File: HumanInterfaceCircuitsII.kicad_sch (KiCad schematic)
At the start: 45 parts

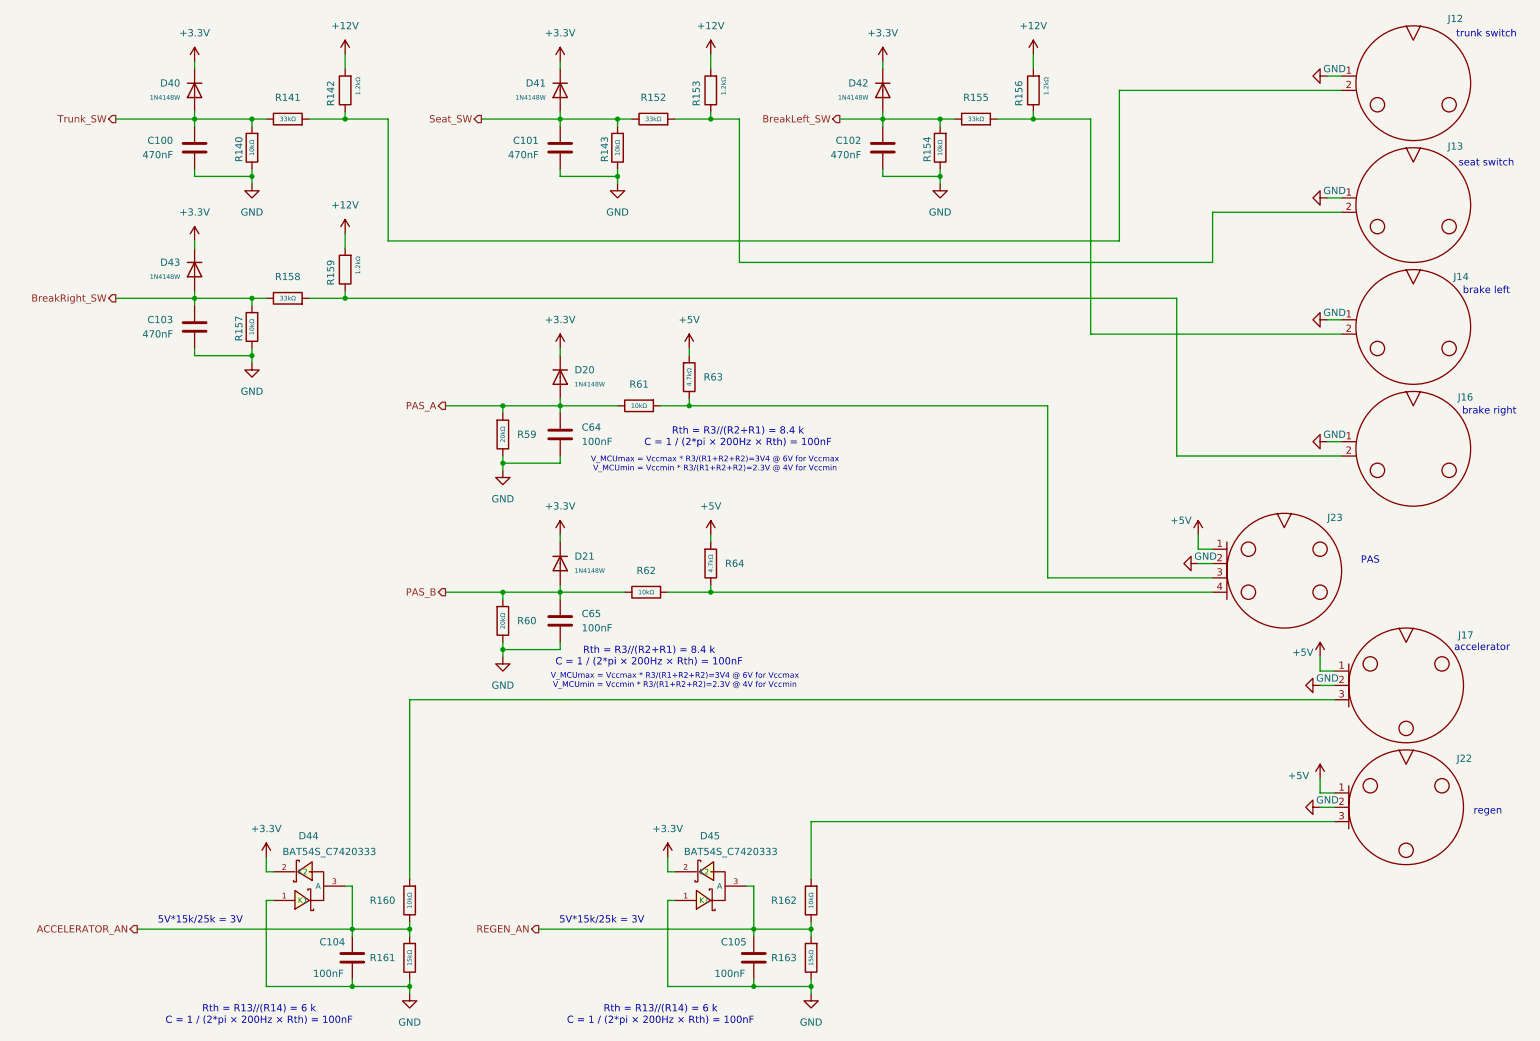
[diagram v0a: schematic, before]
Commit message: EMI/EMC meassures implementation + VCU panel interface block
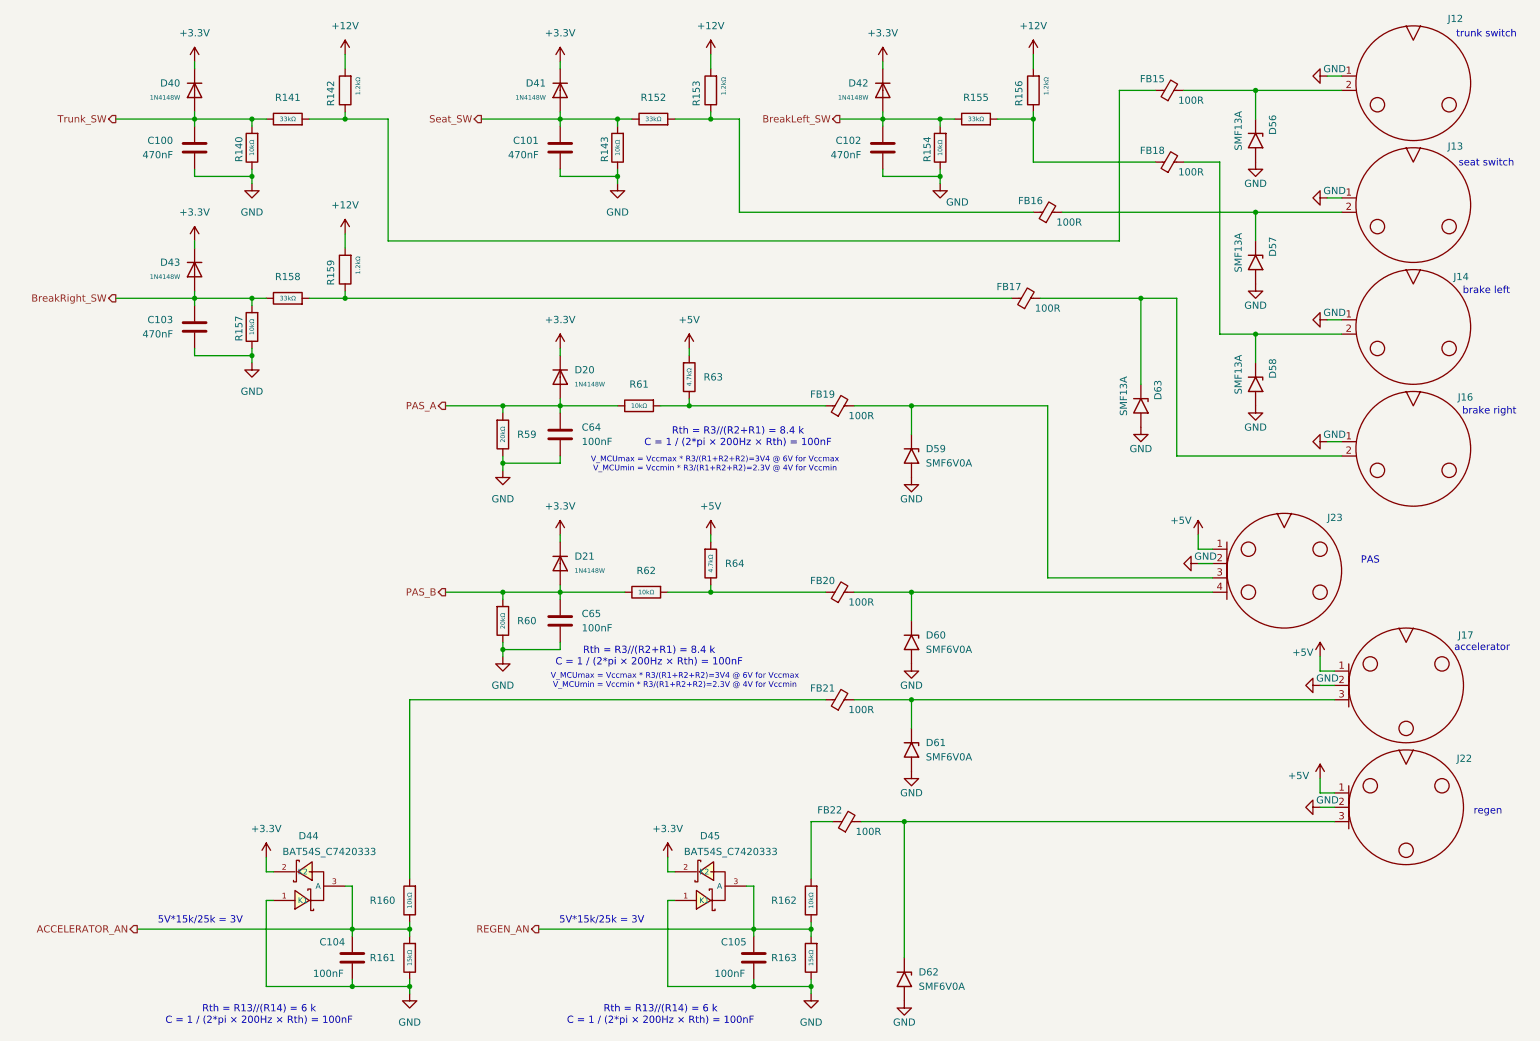
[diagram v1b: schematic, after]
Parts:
- added D56, D57, D58, D63: SMF13A, Diode_SMD:D_SMF, symbol VELION_VCU_Library:SMF13A
- added D59, D60, D61, D62: SMF6V0A, Diode_SMD:D_SMF, symbol VELION_VCU_Library:SMF6V0A
- added FB15, FB16, FB17, FB18, FB19, FB20, FB21, FB22: 100R, Inductor_SMD:L_0603_1608Metric, symbol VELION_VCU_Library:FerriteBead_Small
- C100, C101, C102, C103, C104, C105, C64, C65: footprint (none) -> Capacitor_SMD:C_0603_1608Metric; symbol Device:C -> VELION_VCU_Library:C
- D20, D21, D40, D41, D42, D43: footprint PCM_JLCPCB:D_SOD-123 -> Diode_SMD:D_SOD-123; symbol PCM_JLCPCB-Diodes:Switching,1N4148W -> VELION_VCU_Library:Switching,1N4148W
- D44, D45: footprint PCM_JLCPCB:SOT-23-3_L2.9-W1.3-P1.90-LS2.4-BR -> Package_TO_SOT_SMD:SOT-23-3; symbol PCM_JLCPCB-Diode-Packages:Schottky, BAT54S_C7420333 -> VELION_VCU_Library:Schottky, BAT54S_C7420333
- J12, J13, J14, J16: symbol higo:Z209BM_C_04_00_0000 -> VELION_VCU_Library:Z209BM_C_04_00_0000
- J17, J22: symbol higo:Z309BM_C_04_00_0000 -> VELION_VCU_Library:Z309BM_C_04_00_0000
- J23: symbol higo:Z409BM_C_04_00_0000 -> VELION_VCU_Library:Z409BM_C_04_00_0000
- R140, R143, R154, R157, R160, R162, R61, R62: footprint PCM_JLCPCB:R_0805 -> Resistor_SMD:R_0805_2012Metric; symbol PCM_JLCPCB-Resistors:0805,10kΩ -> VELION_VCU_Library:0805,10kΩ
- R141, R152, R155, R158: footprint PCM_JLCPCB:R_0805 -> Resistor_SMD:R_0805_2012Metric; symbol PCM_JLCPCB-Resistors:0805,33kΩ -> VELION_VCU_Library:0805,33kΩ
- R142, R153, R156, R159: footprint PCM_JLCPCB:R_0805 -> Resistor_SMD:R_0805_2012Metric; symbol PCM_JLCPCB-Resistors:0805,1.2kΩ -> VELION_VCU_Library:0805,1.2kΩ
- R161, R163: footprint PCM_JLCPCB:R_0805 -> Resistor_SMD:R_0805_2012Metric; symbol PCM_JLCPCB-Resistors:0805,15kΩ -> VELION_VCU_Library:0805,15kΩ
- R59, R60: footprint PCM_JLCPCB:R_0805 -> Resistor_SMD:R_0805_2012Metric; symbol PCM_JLCPCB-Resistors:0805,20kΩ -> VELION_VCU_Library:0805,20kΩ
- R63, R64: footprint PCM_JLCPCB:R_0805 -> Resistor_SMD:R_0805_2012Metric; symbol PCM_JLCPCB-Resistors:0805,4.7kΩ -> VELION_VCU_Library:0805,4.7kΩ
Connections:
- net GND: now also D56.2 (A2), D57.2 (A2), D58.2 (A2), D59.2 (A2), D60.2 (A2), D61.2 (A2), D62.2 (A2), D63.2 (A2)
- net at R61.1, R63.2: now also FB19.1; no longer J23.3
- net at R162.1: now also FB22.1; no longer J22.3
- net at R152.1, R153.2: now also FB16.1; no longer J13.2
- net at R62.1, R64.2: now also FB20.1; no longer J23.4
- net at R141.1, R142.2: now also FB15.1; no longer J12.2
- net at R155.1, R156.2: now also FB18.1; no longer J14.2
- net at R158.1, R159.2: now also FB17.1; no longer J16.2
- net at J17.3: now also D61.1 (A1), FB21.2; no longer R160.1
- new net: D60.1 (A1), FB20.2, J23.4
- new net: D57.1 (A1), FB16.2, J13.2
- new net: D59.1 (A1), FB19.2, J23.3
- new net: D58.1 (A1), FB18.2, J14.2
- new net: D62.1 (A1), FB22.2, J22.3
- new net: D63.1 (A1), FB17.2, J16.2
- new net: D56.1 (A1), FB15.2, J12.2
- new net: FB21.1, R160.1
